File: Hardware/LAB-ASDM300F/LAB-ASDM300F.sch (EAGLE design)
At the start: 20 parts, among them U1 TPS62240DRVTG4, U2 MIC94325, U3 MAX4377, X1 C-GRID-04-74099, X2 C-GRID-04-74099

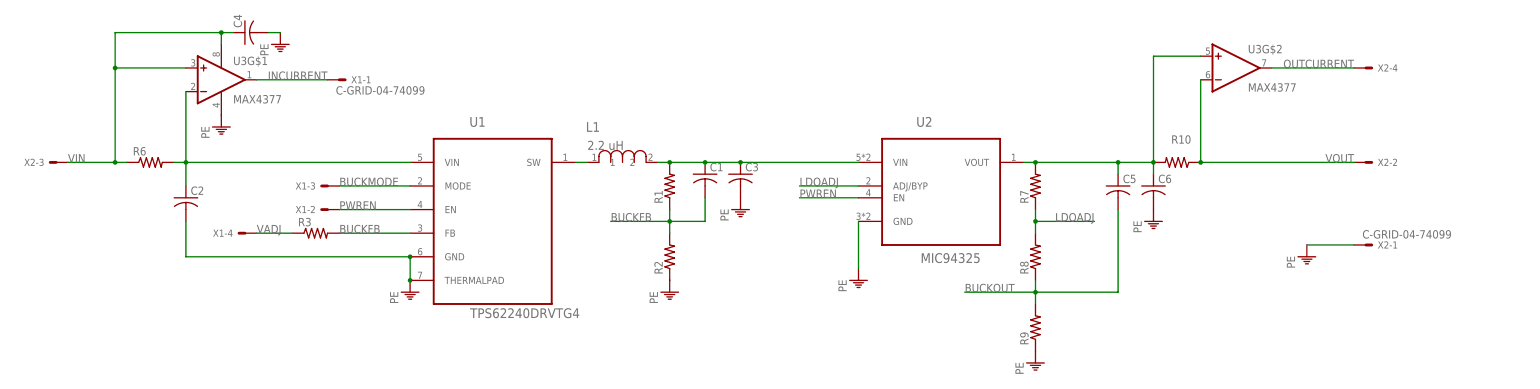
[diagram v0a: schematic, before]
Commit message: 1) Finished the Rev0 board layout ... but its wrong ... (feedback adjustments are messed up -- fixing now)
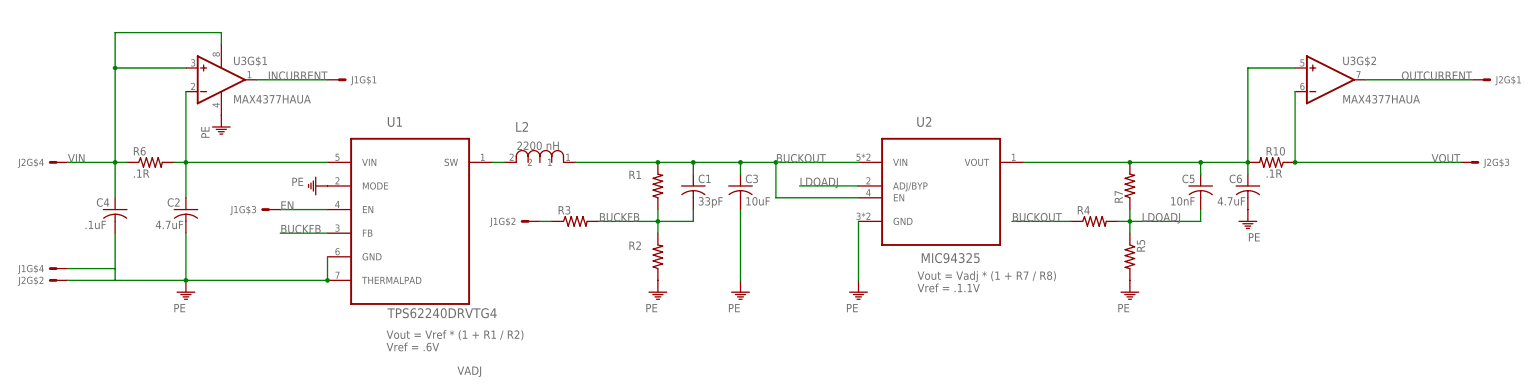
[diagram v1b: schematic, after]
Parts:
- removed L1: 2.2 uH, Bourns_By_element14_Batch_1:PM1210-2R2J-RC
- removed R8, R9: (no value), rcl:R-US_R0402
- removed X1, X2: C-GRID-04-74099, con-molex:C-GRID-04-74099
- added J1, J2: SULLINSSMTHEADER-4, LAB-ASDM300F:SULLINSSMTHEADER-4
- added L2: 2200 nH, Bourns_By_element14_Batch_1:PM1008-2R2K-RC
- added R4, R5: (no value), rcl:R-US_R0603
- C1: value (none) -> 33pF
- C2, C6: value (none) -> 4.7uF
- C3: value (none) -> 10uF
- C4: value (none) -> .1uF
- C5: value (none) -> 10nF
- R1, R2, R3, R7: device rcl:R-US_R0402 -> rcl:R-US_R0603
- R10, R6: value (none) -> .1R; device rcl:R-US_R0402 -> rcl:R-US_R0603
- U3: value MAX4377 -> MAX4377HAUA
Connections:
- removed net BUCKMODE: U1.MODE, X1-3.S
- removed net N$2: C1.1, C3.1, L1.2, R1.2, U2.VIN
- removed net PWREN: U1.EN, U2.EN, X1-2.S
- new net EN: J1G$3.S, U1.EN
- net BUCKOUT: now also C1.1, C3.1, L2.1, R1.2, R4.1, U2.EN, U2.VIN; no longer C5.2, R8.1, R9.2
- net INCURRENT: now also J1G$1.S; no longer X1-1.S
- net LDOADJ: now also C5.2, R4.2, R5.1; no longer R8.2
- net N$1: now also L2.2; no longer L1.1
- net OUTCURRENT: now also J2G$1.S; no longer X2-4.S
- net PE: now also J1G$4.S, J2G$2.S, R5.2, U1.MODE; no longer R9.1, X2-1.S
- net VADJ: now also J1G$2.S; no longer X1-4.S
- net VIN: now also J2G$4.S; no longer X2-3.S
- net VOUT: now also J2G$3.S; no longer X2-2.S
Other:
- note added: "Vout = Vadj * (1 + R7 / R8) Vref = .1.1V"
- note added: "Vout = Vref * (1 + R1 / R2) Vref = .6V"
- moved on the sheet: C1, C2, C3, C4, C5, C6, R1, R10, R2, R3, R7, U1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

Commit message: 1) Revision1 of LAB-ASDM300F 2) Adding ReferenceGuide 3) Removing some autosave crap that should never have been there *) BOM coming soon....
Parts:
- 330K: value (none) -> 360k
- R2: value (none) -> 82k
- R3: value (none) -> 560k
- R4: value (none) -> 220k
- R5: value (none) -> 91k
- R7: value (none) -> 130k
- renumbered R1 to 330K
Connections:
- net BUCKOUT: no longer R4.1
- net VADJ: now also R4.1
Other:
- note added: "LAB304 LLC"
- note added: "NOTE: Vadj must be driven: Vadj = 0.0, Vout = 3.321 Vadj = 3.3, Vout = 1.371"
- moved on the sheet: J1G$2, J2G$1
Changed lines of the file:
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@@
 </classes>
 <parts>
-<part name="FRAME1" library="frames" deviceset="FRAME_B_L" device=""/>
+<part name="FRAME1" library="frames" deviceset="FRAME_B_L" device="" value="LAB304 LLC"/>
 <part name="U1" library="Texas Instruments_By_element14_Batch_1" deviceset="TPS62240DRVTG4" device=""/>
-<part name="R1" library="rcl" deviceset="R-US_" device="R0603"/>
-<part name="R2" library="rcl" deviceset="R-US_" device="R0603"/>
+<part name="330K" library="rcl" deviceset="R-US_" device="R0603" value="360k"/>
+<part name="R2" library="rcl" deviceset="R-US_" device="R0603" value="82k"/>
 <part name="PE1" library="supply1" deviceset="PE" device=""/>
 <part name="C1" library="rcl" deviceset="C-US" device="C0603" value="33pF"/>
@@
 <part name="U2" library="My Library-adm" deviceset="MIC94325" device=""/>
 <part name="PE5" library="supply1" deviceset="PE" device=""/>
-<part name="R7" library="rcl" deviceset="R-US_" device="R0603"/>
+<part name="R7" library="rcl" deviceset="R-US_" device="R0603" value="130k"/>
 <part name="PE6" library="supply1" deviceset="PE" device=""/>
 <part name="C5" library="rcl" deviceset="C-US" device="C0603" value="10nF"/>
@@
 <part name="R10" library="rcl" deviceset="R-US_" device="R0603" value=".1R"/>
 <part name="PE9" library="supply1" deviceset="PE" device=""/>
-<part name="R3" library="rcl" deviceset="R-US_" device="R0603"/>
+<part name="R3" library="rcl" deviceset="R-US_" device="R0603" value="560k"/>
 <part name="L2" library="Bourns_By_element14_Batch_1" deviceset="PM1008-2R2K-RC" device="" value="2200 nH"/>
 <part name="PE10" library="supply1" deviceset="PE" device=""/>
@@
 <part name="J2" library="LAB-ASDM300F" deviceset="SULLINSSMTHEADER-4" device=""/>
 <part name="PE2" library="supply1" deviceset="PE" device=""/>
-<part name="R4" library="rcl" deviceset="R-US_" device="R0603"/>
-<part name="R5" library="rcl" deviceset="R-US_" device="R0603"/>
+<part name="R4" library="rcl" deviceset="R-US_" device="R0603" value="220k"/>
+<part name="R5" library="rcl" deviceset="R-US_" device="R0603" value="91k"/>
 </parts>
 <sheets>
@@
 <text x="261.62" y="154.94" size="1.778" layer="95">Vout = Vadj * (1 + R7 / R8)
 Vref = .1.1V</text>
+<text x="175.26" y="213.36" size="5.08" layer="95">NOTE: Vadj must be driven:
+Vadj = 0.0, Vout = 3.321
+Vadj = 3.3, Vout = 1.371</text>
+<text x="355.6" y="25.4" size="5.08" layer="94">LAB304 LLC</text>
 </plain>
 <instances>
@@
 <attribute name="VALUE" x="147.5232" y="149.3774" size="2.0828" layer="96" ratio="10" rot="SR0"/>
 </instance>
-<instance part="R1" gate="G$1" x="205.74" y="177.8" smashed="yes" rot="R90">
-<attribute name="NAME" x="199.39" y="179.2986" size="1.778" layer="95"/>
-<attribute name="VALUE" x="209.042" y="173.99" size="1.778" layer="96" rot="R90"/>
+<instance part="330K" gate="G$1" x="205.74" y="177.8" smashed="yes" rot="R90">
+<attribute name="NAME" x="204.47" y="179.2986" size="1.778" layer="95" rot="MR0"/>
+<attribute name="VALUE" x="204.47" y="177.038" size="1.778" layer="96" rot="MR0"/>
 </instance>
 <instance part="R2" gate="G$1" x="205.74" y="162.56" smashed="yes" rot="R90">
-<attribute name="NAME" x="199.39" y="164.0586" size="1.778" layer="95"/>
-<attribute name="VALUE" x="209.042" y="158.75" size="1.778" layer="96" rot="R90"/>
+<attribute name="NAME" x="204.47" y="164.0586" size="1.778" layer="95" rot="MR0"/>
+<attribute name="VALUE" x="204.47" y="161.798" size="1.778" layer="96" rot="MR0"/>
 </instance>
 <instance part="PE1" gate="M" x="205.74" y="154.94" smashed="yes">
@@
 </instance>
 <instance part="R7" gate="G$1" x="307.34" y="177.8" smashed="yes" rot="R90">
-<attribute name="NAME" x="305.8414" y="173.99" size="1.778" layer="95" rot="R90"/>
-<attribute name="VALUE" x="310.642" y="173.99" size="1.778" layer="96" rot="R90"/>
+<attribute name="NAME" x="306.07" y="176.7586" size="1.778" layer="95" rot="MR0"/>
+<attribute name="VALUE" x="306.07" y="174.498" size="1.778" layer="96" rot="MR0"/>
 </instance>
 <instance part="PE6" gate="M" x="307.34" y="154.94" smashed="yes">
@@
 <attribute name="NAME" x="139.7" y="199.898" size="1.524" layer="95"/>
 </instance>
-<instance part="J1" gate="G$2" x="177.8" y="170.18" smashed="yes" rot="R180">
-<attribute name="NAME" x="175.26" y="170.942" size="1.524" layer="95" rot="R180"/>
+<instance part="J1" gate="G$2" x="210.82" y="203.2" smashed="yes" rot="R180">
+<attribute name="NAME" x="208.28" y="203.962" size="1.524" layer="95" rot="R180"/>
 </instance>
 <instance part="J1" gate="G$3" x="121.92" y="172.72" smashed="yes" rot="R180">
@@
 <attribute name="NAME" x="73.66" y="160.782" size="1.524" layer="95" rot="R180"/>
 </instance>
-<instance part="J2" gate="G$1" x="383.54" y="200.66" smashed="yes" rot="MR180">
-<attribute name="NAME" x="386.08" y="201.422" size="1.524" layer="95" rot="MR180"/>
+<instance part="J2" gate="G$1" x="381" y="200.66" smashed="yes" rot="MR180">
+<attribute name="NAME" x="383.54" y="201.422" size="1.524" layer="95" rot="MR180"/>
 </instance>
 <instance part="J2" gate="G$2" x="76.2" y="157.48" smashed="yes" rot="MR0">
@@
 </instance>
 <instance part="R5" gate="G$1" x="307.34" y="162.56" smashed="yes" rot="R270">
-<attribute name="NAME" x="308.8386" y="166.37" size="1.778" layer="95" rot="R270"/>
-<attribute name="VALUE" x="304.038" y="166.37" size="1.778" layer="96" rot="R270"/>
+<attribute name="NAME" x="306.07" y="161.5186" size="1.778" layer="95" rot="MR0"/>
+<attribute name="VALUE" x="306.07" y="159.258" size="1.778" layer="96" rot="MR0"/>
 </instance>
 </instances>
@@
 <net name="BUCKFB" class="0">
 <segment>
-<pinref part="R1" gate="G$1" pin="1"/>
+<pinref part="330K" gate="G$1" pin="1"/>
 <pinref part="R2" gate="G$1" pin="2"/>
 <wire x1="205.74" y1="172.72" x2="205.74" y2="170.18" width="0.1524" layer="91"/>
@@
 <net name="BUCKOUT" class="0">
 <segment>
-<pinref part="R1" gate="G$1" pin="2"/>
+<pinref part="330K" gate="G$1" pin="2"/>
 <wire x1="187.96" y1="182.88" x2="205.74" y2="182.88" width="0.1524" layer="91"/>
 <junction x="205.74" y="182.88"/>
@@
 <junction x="223.52" y="182.88"/>
 </segment>
-<segment>
-<pinref part="R4" gate="G$1" pin="1"/>
-<wire x1="294.64" y1="170.18" x2="281.94" y2="170.18" width="0.1524" layer="91"/>
-<label x="281.94" y="170.18" size="1.778" layer="95"/>
-</segment>
 </net>
 <net name="VOUT" class="0">
@@
 <segment>
 <pinref part="U3" gate="G$2" pin="OUT"/>
-<wire x1="381" y1="200.66" x2="358.14" y2="200.66" width="0.1524" layer="91"/>
+<wire x1="378.46" y1="200.66" x2="358.14" y2="200.66" width="0.1524" layer="91"/>
 <pinref part="J2" gate="G$1" pin="S"/>
-<label x="381" y="200.66" size="1.778" layer="95" rot="MR0"/>
-</segment>
-</net>
-<net name="VADJ" class="0">
-<segment>
-<pinref part="R3" gate="G$1" pin="1"/>
-<wire x1="180.34" y1="170.18" x2="182.88" y2="170.18" width="0.1524" layer="91"/>
-<label x="162.56" y="137.16" size="1.778" layer="95"/>
-<pinref part="J1" gate="G$2" pin="S"/>
+<label x="378.46" y="200.66" size="1.778" layer="95" rot="MR0"/>
 </segment>
 </net>
@@
 </segment>
 </net>
+<net name="VADJ" class="0">
+<segment>
+<pinref part="J1" gate="G$2" pin="S"/>
+<wire x1="213.36" y1="203.2" x2="223.52" y2="203.2" width="0.1524" layer="91"/>
+<label x="223.52" y="203.2" size="1.778" layer="95" rot="MR0"/>
+</segment>
+<segment>
+<pinref part="R3" gate="G$1" pin="1"/>
+<wire x1="182.88" y1="170.18" x2="172.72" y2="170.18" width="0.1524" layer="91"/>
+<label x="172.72" y="170.18" size="1.778" layer="95"/>
+</segment>
+<segment>
+<pinref part="R4" gate="G$1" pin="1"/>
+<wire x1="294.64" y1="170.18" x2="284.48" y2="170.18" width="0.1524" layer="91"/>
+<label x="284.48" y="170.18" size="1.778" layer="95"/>
+</segment>
+</net>

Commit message: 1) Finished the Rev1 BOM 2) R1 was inadvertently named 330k, changed the designator and bumped the rev. Sticking with Rev2 until new boards go out -- changes may be necessary ...
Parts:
- R1: value 360k -> 330k
- renumbered 330K to R1
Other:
- note added: "2"
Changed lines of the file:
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@@
 <?xml version="1.0" encoding="utf-8"?>
 <!DOCTYPE eagle SYSTEM "eagle.dtd">
-<eagle version="6.5.0">
+<eagle version="6.6.0">
 <drawing>
 <settings>
@@
 <part name="FRAME1" library="frames" deviceset="FRAME_B_L" device="" value="LAB304 LLC"/>
 <part name="U1" library="Texas Instruments_By_element14_Batch_1" deviceset="TPS62240DRVTG4" device=""/>
-<part name="330K" library="rcl" deviceset="R-US_" device="R0603" value="360k"/>
+<part name="R1" library="rcl" deviceset="R-US_" device="R0603" value="330k"/>
 <part name="R2" library="rcl" deviceset="R-US_" device="R0603" value="82k"/>
 <part name="PE1" library="supply1" deviceset="PE" device=""/>
@@
 Vadj = 3.3, Vout = 1.371</text>
 <text x="355.6" y="25.4" size="5.08" layer="94">LAB304 LLC</text>
+<text x="419.1" y="7.62" size="1.778" layer="94">2</text>
 </plain>
 <instances>
@@
 <attribute name="VALUE" x="147.5232" y="149.3774" size="2.0828" layer="96" ratio="10" rot="SR0"/>
 </instance>
-<instance part="330K" gate="G$1" x="205.74" y="177.8" smashed="yes" rot="R90">
+<instance part="R1" gate="G$1" x="205.74" y="177.8" smashed="yes" rot="R90">
 <attribute name="NAME" x="204.47" y="179.2986" size="1.778" layer="95" rot="MR0"/>
 <attribute name="VALUE" x="204.47" y="177.038" size="1.778" layer="96" rot="MR0"/>
@@
 <net name="BUCKFB" class="0">
 <segment>
-<pinref part="330K" gate="G$1" pin="1"/>
+<pinref part="R1" gate="G$1" pin="1"/>
 <pinref part="R2" gate="G$1" pin="2"/>
 <wire x1="205.74" y1="172.72" x2="205.74" y2="170.18" width="0.1524" layer="91"/>
@@
 <net name="BUCKOUT" class="0">
 <segment>
-<pinref part="330K" gate="G$1" pin="2"/>
+<pinref part="R1" gate="G$1" pin="2"/>
 <wire x1="187.96" y1="182.88" x2="205.74" y2="182.88" width="0.1524" layer="91"/>
 <junction x="205.74" y="182.88"/>
